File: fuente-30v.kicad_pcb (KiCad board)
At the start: 2 copper layers, 30 parts, among them P1 POT, P2 POT, Q1-CONN1 CONN_01X03, Q2 BD137, Q3 BD139, Q4 BC167, Q5 BC167, T1 TRANSFO, con3 CONN_01X02

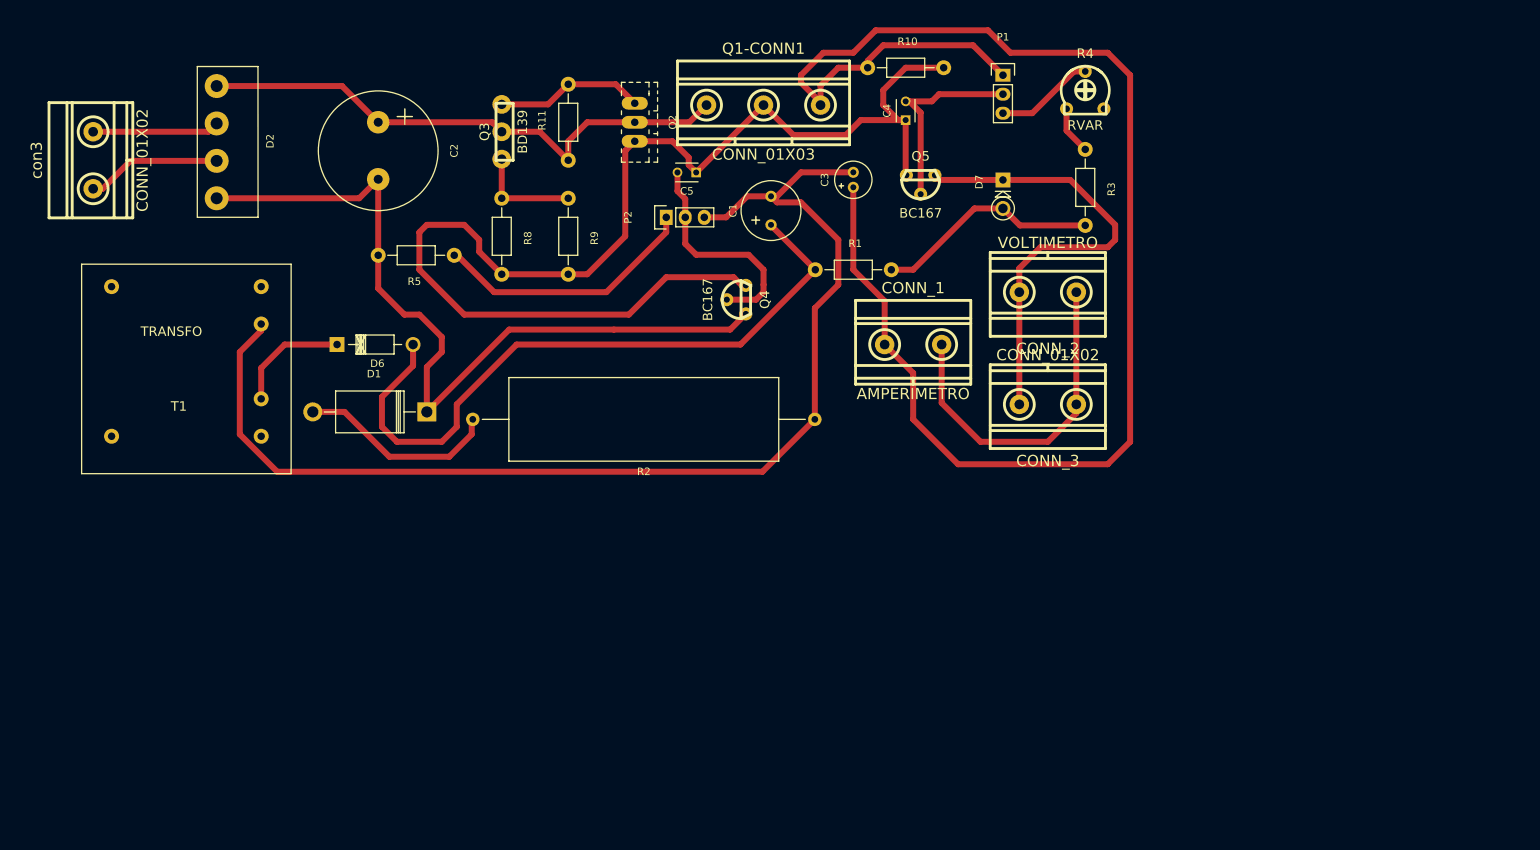
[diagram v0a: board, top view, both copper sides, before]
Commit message: version 1.1: arreglados los problemas de conexion
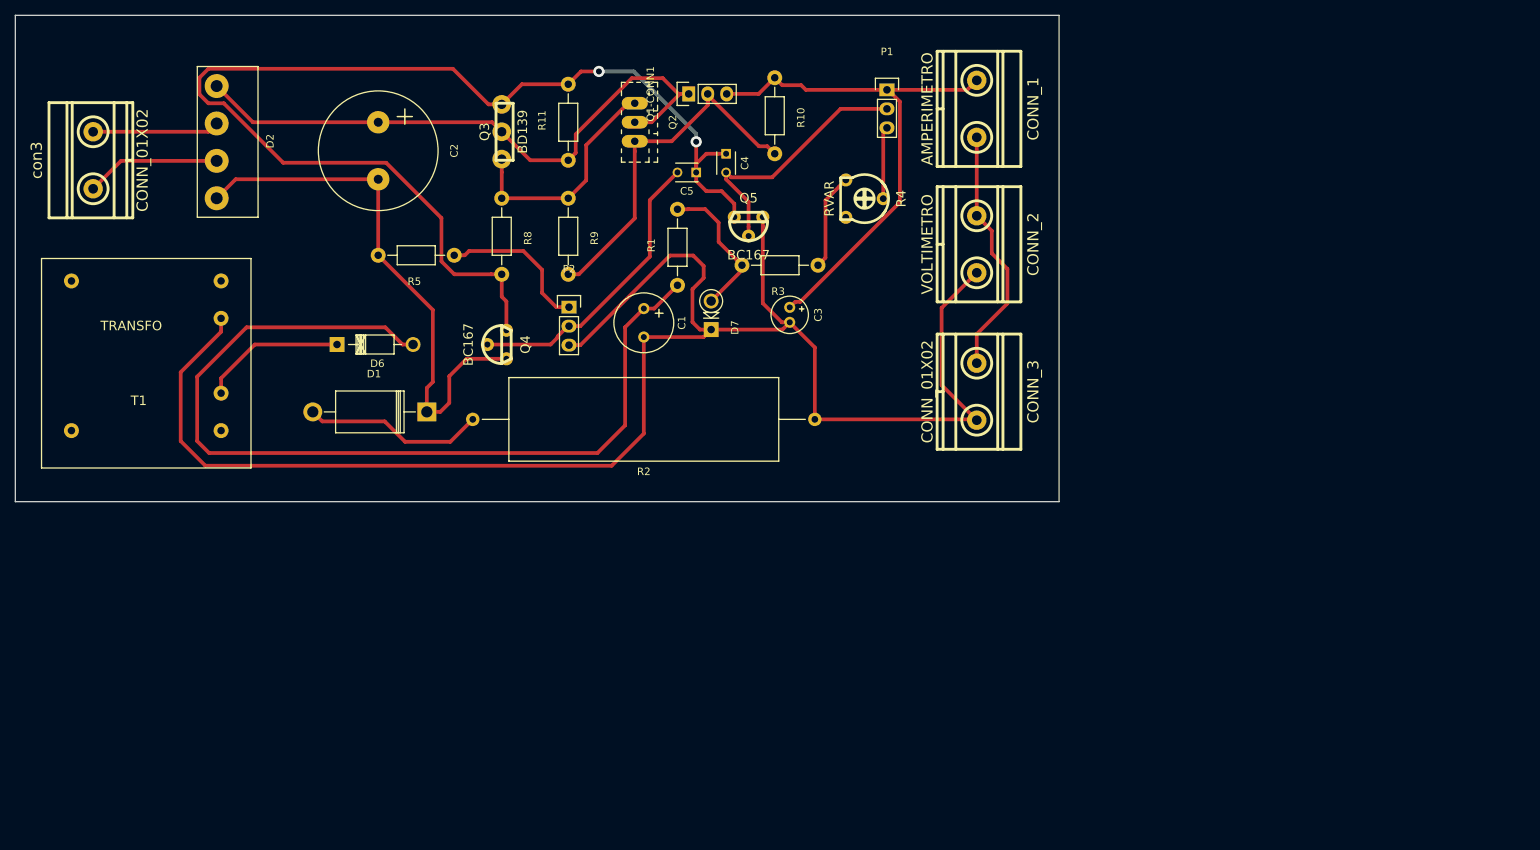
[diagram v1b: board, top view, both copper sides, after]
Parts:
- Q1-CONN1: footprint w_conn_gmkds:gmkds_3-3-7,62 -> Pin_Headers:Pin_Header_Straight_1x03
- moved D7 43.8 mm to (108.0, 62.0), turned to 90 degrees
- moved R3 42.1 mm to (117.2, 53.4), turned to 180 degrees
- moved R4 32.9 mm to (128.5, 44.5), turned to 90 degrees
- moved CONN_1 32.6 mm to (143.5, 32.5), turned to 270 degrees
- moved Q4 32.6 mm to (80.0, 64.0)
- moved C4 24.4 mm to (110.0, 38.5), turned to 270 degrees
- moved R1 23.7 mm to (103.5, 51.0), turned to 90 degrees
- moved Q5 23.7 mm to (113.0, 47.6)
- moved C1 20.4 mm to (99.0, 59.2), turned to 270 degrees
- moved R10 18.6 mm to (116.5, 33.4), turned to 270 degrees
- moved C3 18.1 mm to (118.5, 59.0), turned to 270 degrees
- moved P2 17.7 mm to (89.0, 59.0), turned to 0 degrees
- moved P1 15.6 mm to (131.5, 30.0)
- moved CONN_2 11.5 mm to (143.5, 50.6), turned to 270 degrees
- moved Q1-CONN1 10.1 mm to (105.0, 30.5), turned to 90 degrees
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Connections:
- Q1-CONN1 pad 2: 1 -> Net-(Q1-CONN1-Pad2)
- Q2 pad 1: 1 -> Net-(Q1-CONN1-Pad2)
- Q3 pad 3: Net-(Q2-Pad3) -> 1
- R10 pad 2: 1 -> Net-(Q1-CONN1-Pad2)
- R11 pad 2: Net-(Q2-Pad3) -> 1
- R9 pad 2: 1 -> Net-(Q1-CONN1-Pad2)
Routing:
- net Net-(C3-Pad1): track 201.5 -> 71.9 mm
- net Net-(Q1-CONN1-Pad2): track 0.00 -> 47.9 mm
- net Net-(C2-Pad2): track 108.3 -> 72.8 mm
- net Net-(C1-Pad1): track 92.1 -> 123.0 mm
- net Net-(P2-Pad1): track 36.3 -> 20.5 mm
- net Net-(CONN_1-Pad2): track 45.7 -> 33.6 mm
- net Net-(D7-Pad2): track 30.3 -> 19.7 mm
- net 1: track 167.9 -> 158.0 mm, vias 0 -> 2
- net Net-(C5-Pad2): track 30.2 -> 39.4 mm
- net A: track 218.3 -> 227.3 mm
- net Net-(C4-Pad2): track 26.9 -> 35.8 mm
- net Net-(C2-Pad1): track 74.1 -> 81.8 mm
- net Net-(R3-Pad1): track 6.46 -> 12.9 mm
- net F: track 15.6 -> 19.4 mm
- net Net-(P1-Pad3): track 13.3 -> 9.67 mm
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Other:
- board outline added: 139.5 x 65 mm
- net class Default: clearance 0.2 -> 0.4572; trace_width 0.25 -> 0.3556; via_dia 0.6 -> 1.5; via_drill 0.4 -> 0.8
- rule trace_clearance: 0.2 -> 0.4572
- rule trace_min: 0.2 -> 0.3048
- rule via_min_drill: 0.3 -> 0.8
- rule via_min_size: 0.4 -> 1.5

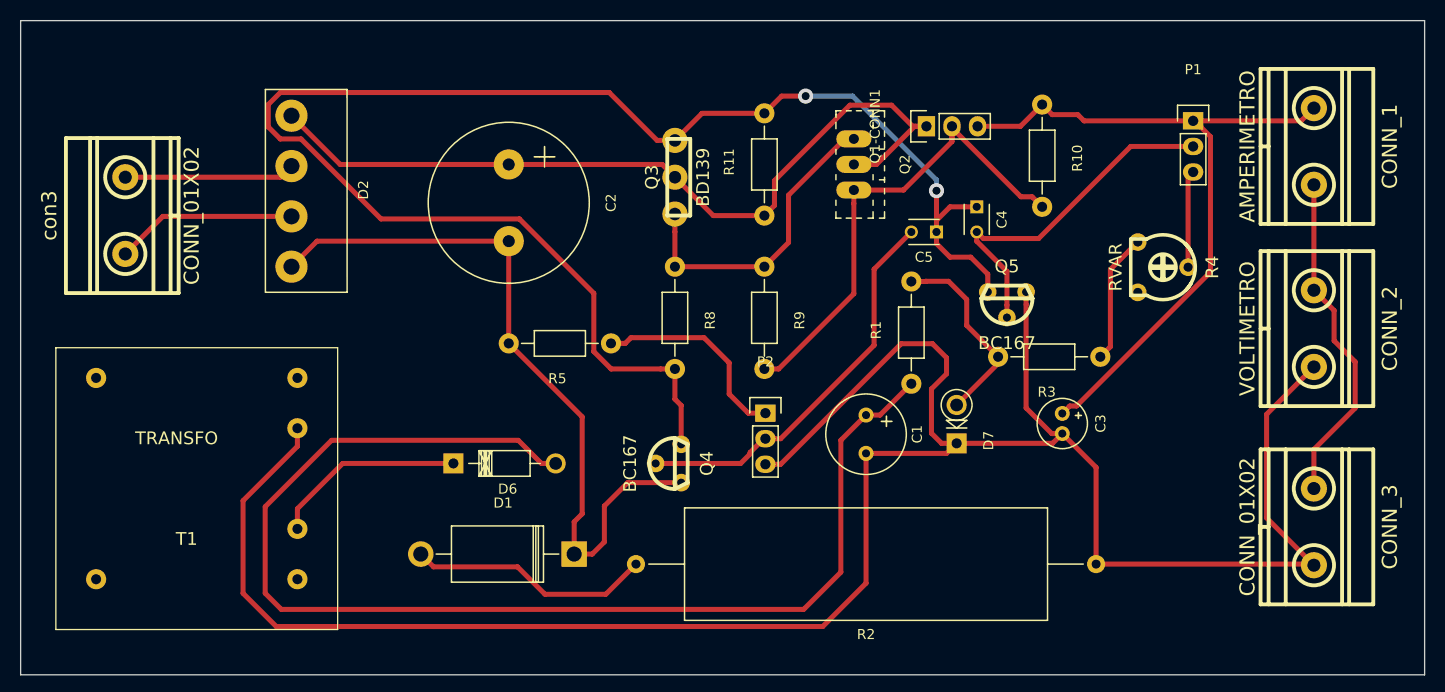
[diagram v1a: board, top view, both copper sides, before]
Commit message: change track width to 1 mm
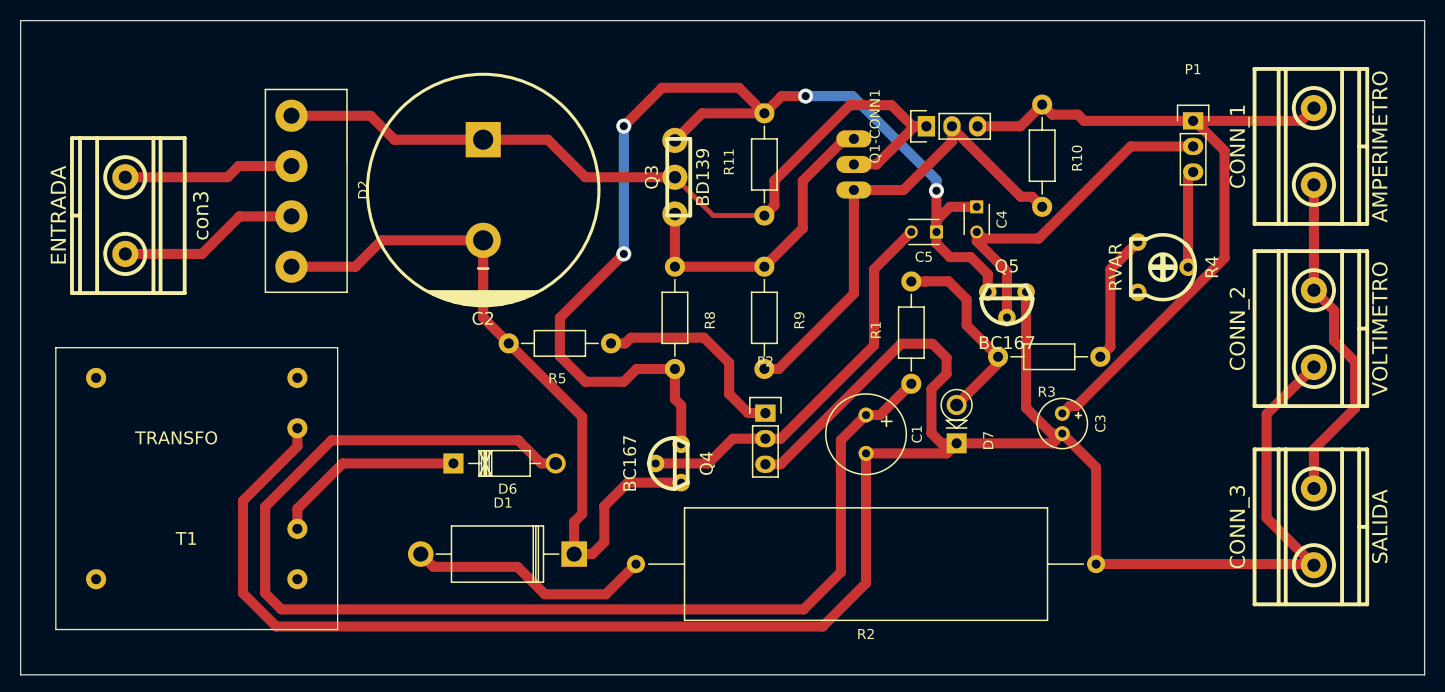
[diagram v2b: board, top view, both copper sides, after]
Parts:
- C2: footprint Capacitors_Elko_ThroughHole:Elko_vert_31.5x16mm_RM7.5 -> w_capacitors:CP_22x25mm
- CONN_3: value CONN_01X02 -> SALIDA
- P1: value POT -> POT_1
- P2: value POT -> POT_2
- Q1-CONN1: value CONN_01X03 -> 2N3055
- Q2: moved to B.Cu
- con3: value CONN_01X02 -> ENTRADA
- moved C2 3.59 mm to (61.0, 36.8), turned to 180 degrees
- turned CONN_1 to 90 degrees
- turned CONN_2 to 90 degrees
- turned CONN_3 to 90 degrees
- turned con3 to 270 degrees
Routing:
- net 1: track 158.0 -> 114.3 mm, vias 2 -> 4
- net Net-(C2-Pad2): track 72.8 -> 71.4 mm
- net Net-(C3-Pad1): track 71.9 -> 73.0 mm

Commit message: checked and fixed design rules
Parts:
- P1: value POT_1 -> POT
- P2: value POT_2 -> POT
- Q1-CONN1: value 2N3055 -> CONN_01X03
- moved C2 76.5 mm to (123.2, 81.3)
- moved D2 76.5 mm to (104.1, 88.9)
- moved D6 76.5 mm to (120.2, 108.5)
- moved Q2 76.5 mm to (160.0, 78.7)
- moved Q3 76.5 mm to (142.2, 80.0)
- moved R3 76.5 mm to (179.4, 97.8)
- moved R5 76.5 mm to (130.8, 96.5)
- moved R8 76.5 mm to (142.2, 94.0)
- moved T1 76.5 mm to (79.7, 92.0)
- moved C1 76.5 mm to (161.2, 103.6)
- moved C4 76.5 mm to (172.2, 83.0)
- moved C5 76.5 mm to (168.2, 85.5)
- moved CONN_1 76.5 mm to (205.7, 77.0)
- moved CONN_3 76.5 mm to (205.7, 114.8)
- moved CONN_4 76.5 mm to (87.6, 83.8)
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- renumbered con3 to CONN_4
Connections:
- T1 pad 1: (no net) -> Net-(D2-Pad4)
- T1 pad 5: (no net) -> Net-(D2-Pad2)
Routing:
- net Net-(D2-Pad4): track 17.0 -> 61.0 mm
- net Net-(D2-Pad2): track 18.1 -> 31.6 mm
- net Net-(C3-Pad1): track 73.0 -> 78.0 mm
- net 1: track 114.3 -> 117.9 mm
- net Net-(Q2-Pad3): track 31.0 -> 33.6 mm
- net Net-(C2-Pad1): track 81.8 -> 84.1 mm
- net Net-(Q1-CONN1-Pad2): track 47.9 -> 48.6 mm
